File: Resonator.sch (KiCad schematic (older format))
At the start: 6 parts, among them U1 PCM3060

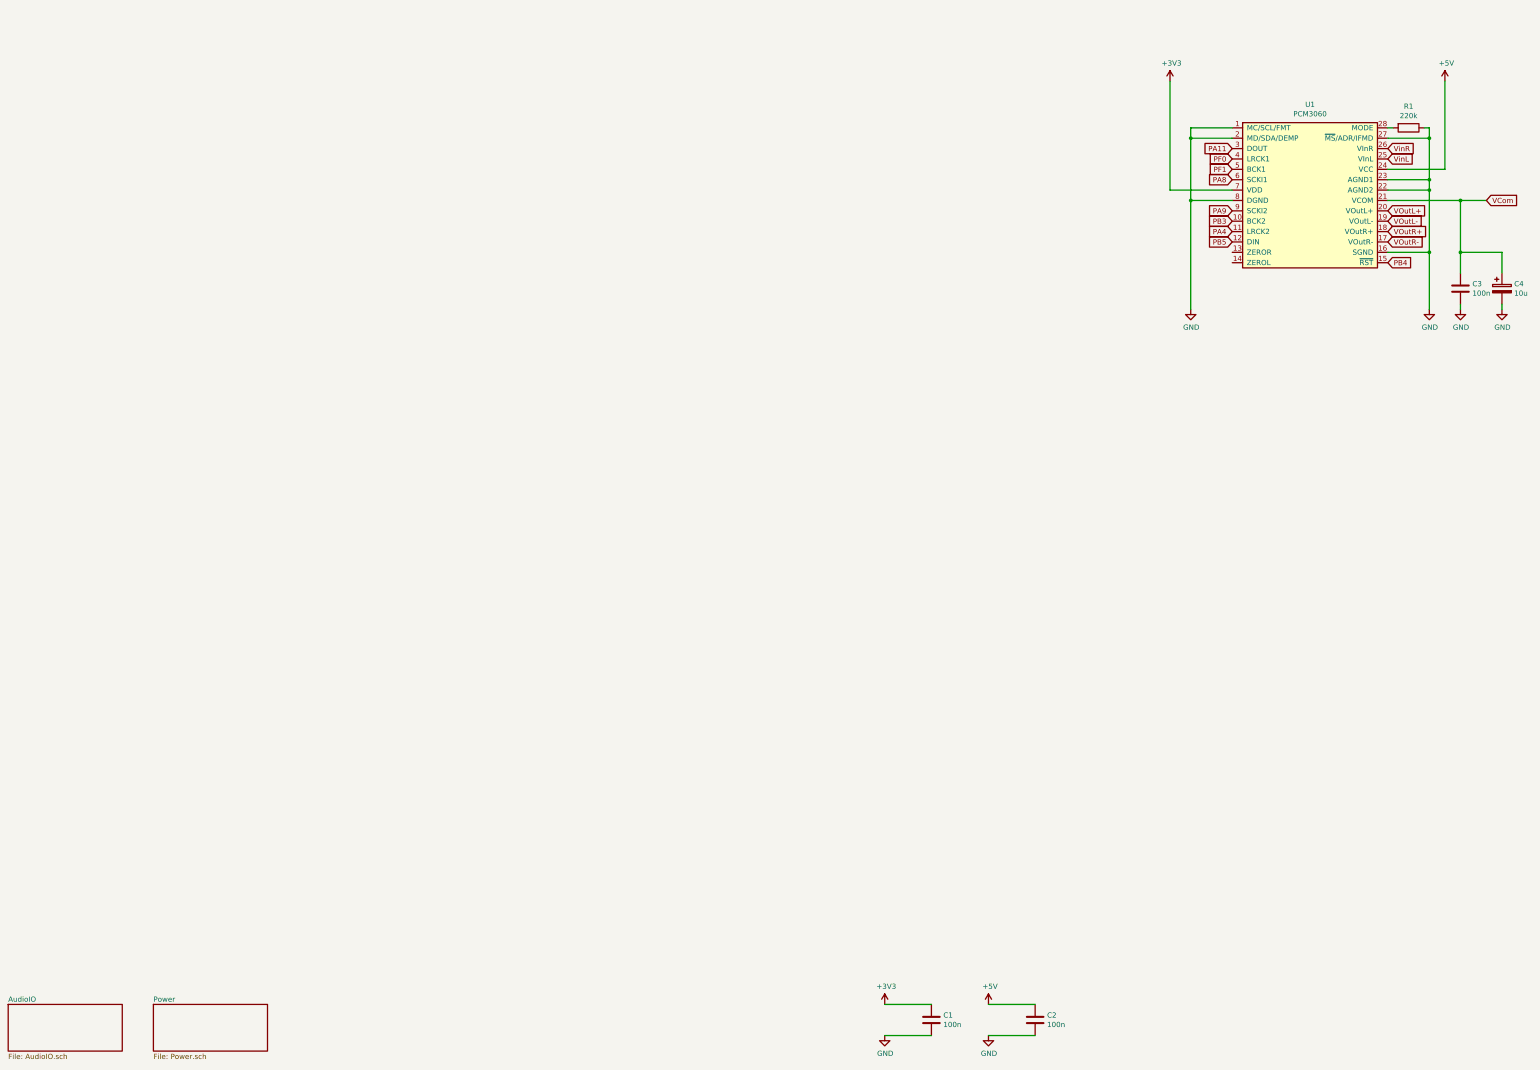
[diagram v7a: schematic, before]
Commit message: Added STM32750 mcu.
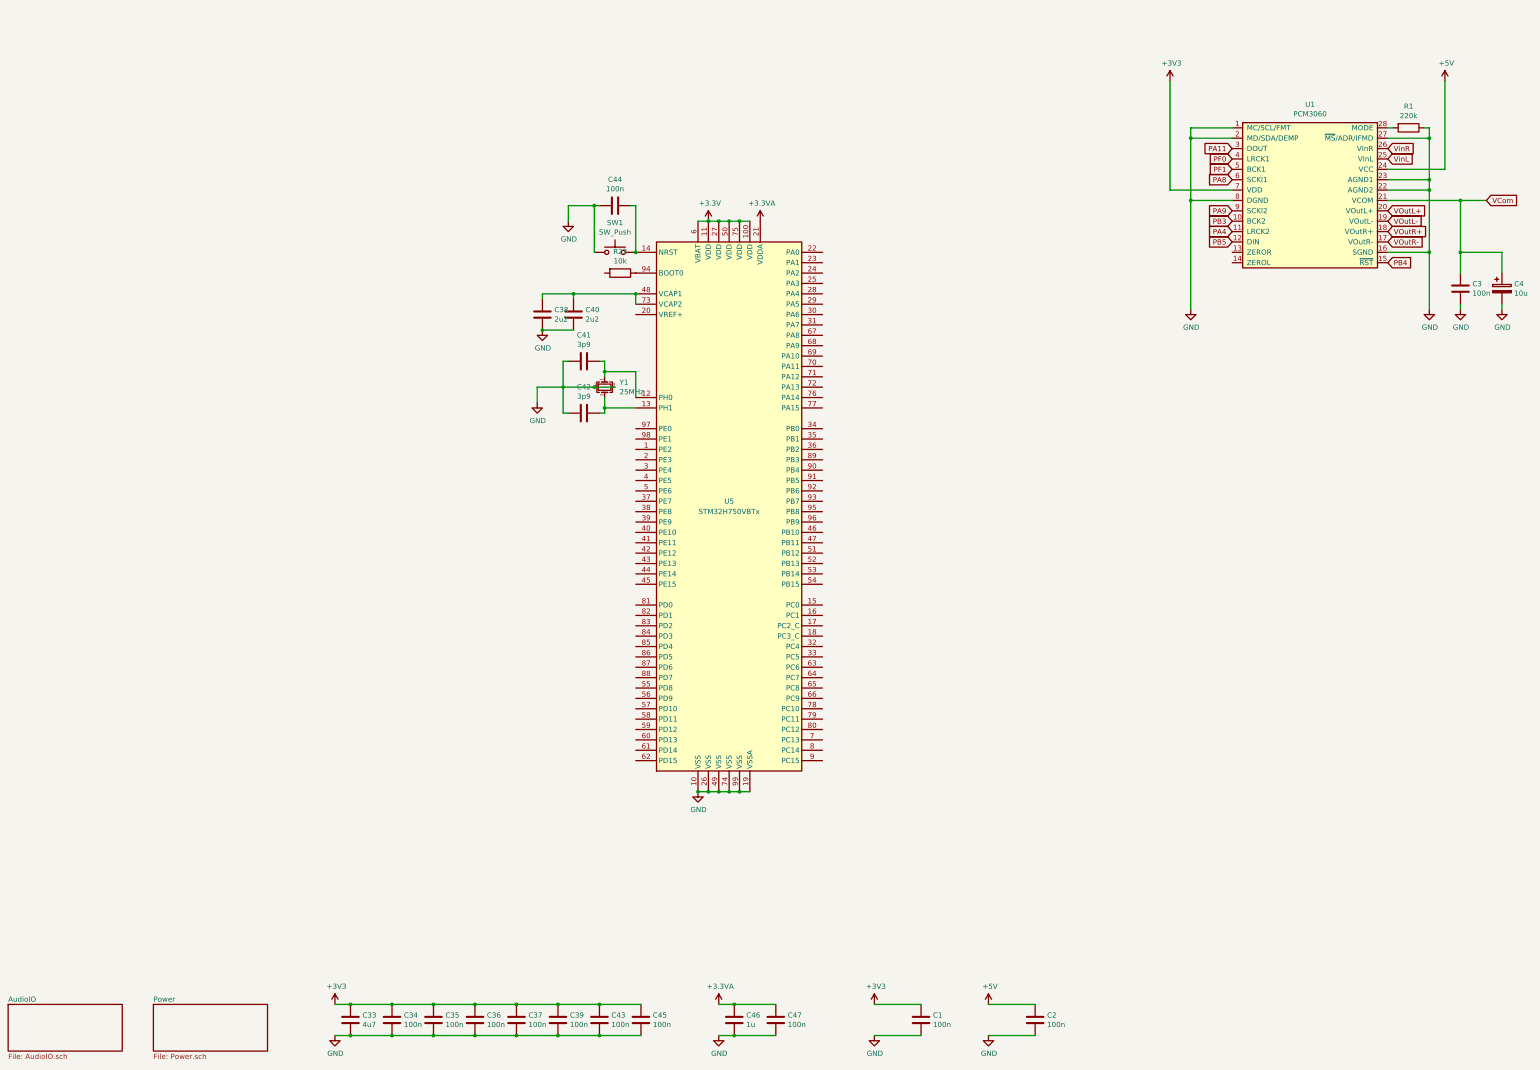
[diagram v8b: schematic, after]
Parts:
- added C33: 4u7, Capacitor_SMD:C_0805_2012Metric, symbol Device:C
- added C34, C35, C36, C37, C39, C43, C44, C45, C47: 100n, Capacitor_SMD:C_0603_1608Metric, symbol Device:C
- added C38, C40: 2u2, Capacitor_SMD:C_0805_2012Metric, symbol Device:C
- added C41, C42: 3p9, Capacitor_SMD:C_0603_1608Metric, symbol Device:C
- added C46: 1u, Capacitor_SMD:C_0805_2012Metric, symbol Device:C
- added R23: 10k, Resistor_SMD:R_0603_1608Metric, symbol Device:R
- added SW1: SW_Push, symbol Switch:SW_Push
- added U5: STM32H750VBTx, Package_QFP:LQFP-100_14x14mm_P0.5mm, symbol MCU_ST_STM32H7:STM32H750VBTx
- added Y1: 25MHz, symbol Device:Crystal_GND24_Small
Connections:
- net +3V3: now also C33.1, C34.1, C35.1, C36.1, C37.1, C39.1, C43.1, C45.1, U5.100 (VDD), U5.11 (VDD), U5.27 (VDD), U5.50 (VDD), U5.6 (VBAT), U5.75 (VDD)
- net GND: now also C33.2, C34.2, C35.2, C36.2, C37.2, C38.2, C39.2, C40.2, C41.2, C42.2, C43.2, C44.2, C45.2, C46.2, C47.2, SW1.1, U5.10 (VSS), U5.19 (VSSA), U5.26 (VSS), U5.49 (VSS), U5.74 (VSS), U5.99 (VSS), Y1.2, Y1.4
- new net: C41.1, U5.12 (PH0), Y1.1
- new net: C42.1, U5.13 (PH1), Y1.3
- new net: C44.1, SW1.2, U5.14 (NRST)
- new net: C38.1, C40.1, U5.48 (VCAP1), U5.73 (VCAP2)
- new net: R23.1, U5.94 (BOOT0)
- new net +3.3VA: C46.1, C47.1, U5.21 (VDDA)
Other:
- moved on the sheet: C1
